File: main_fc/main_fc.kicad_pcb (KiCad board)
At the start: 2 copper layers, 198 parts, among them U1 ADS1158IRTCR, U10 AD8495, U11 AD8495, U12 AD8495, U13 AD8495, U14 AD8495, U15 AD8495, U2 AD8495, U3 OP777ARZ, U4 STM32H730ZBTx, U6 LAN8742A, U7 FT232RL, U8 ADS1158IRTCR, U9 AD8495

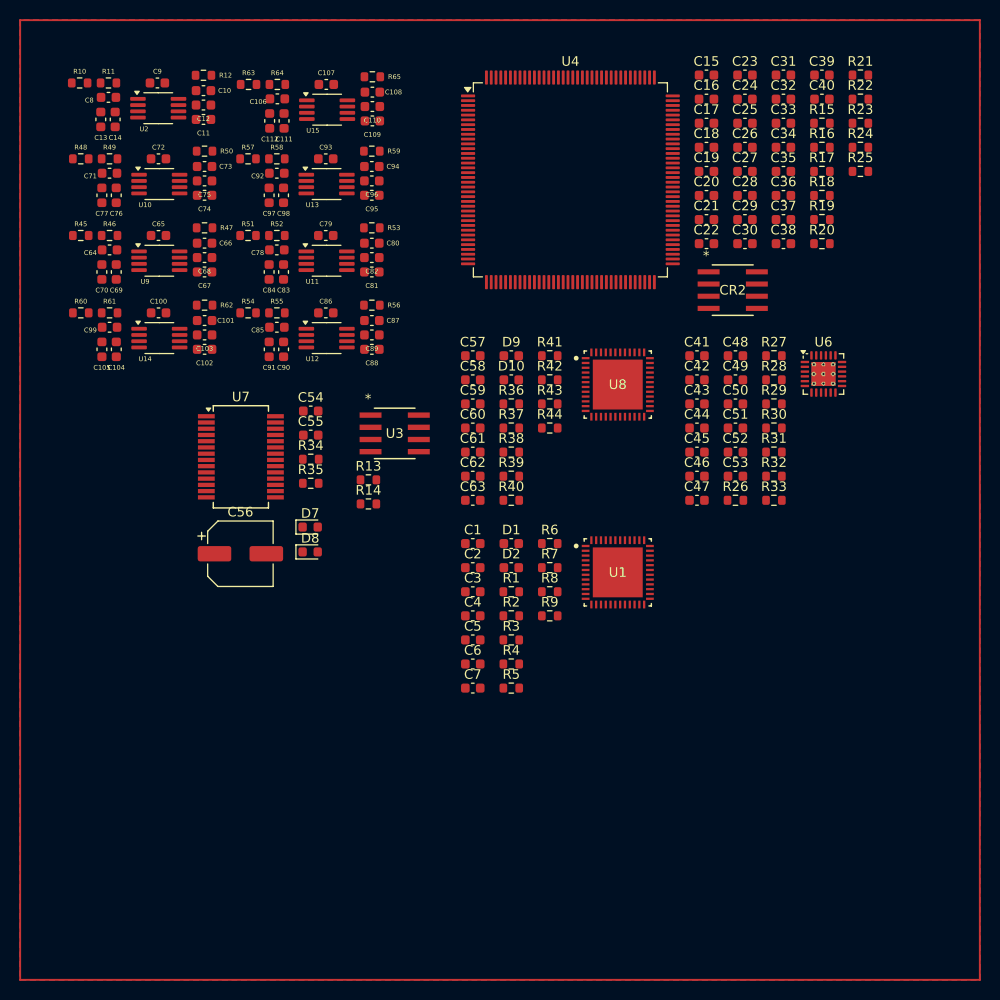
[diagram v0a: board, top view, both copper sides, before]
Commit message: added new stm symbol/footprint
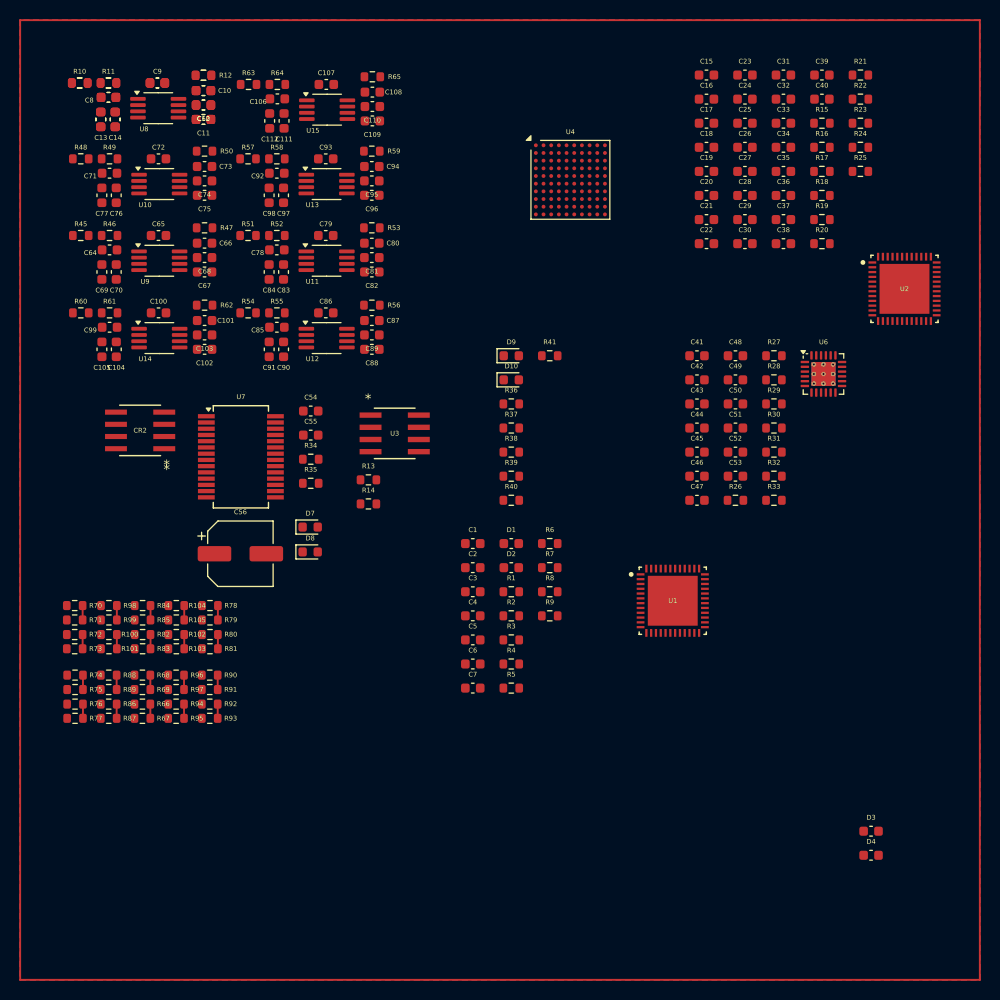
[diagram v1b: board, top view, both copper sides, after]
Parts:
- added D3: LED, Capacitor_SMD:C_0603_1608Metric, F.Cu at (121.7, 113.3)
- added D4: LED, Capacitor_SMD:C_0603_1608Metric, F.Cu at (121.7, 115.8)
- added R100: 2k, Resistor_SMD:R_0603_1608Metric, F.Cu at (42.2, 92.8)
- added R101: 1k, Resistor_SMD:R_0603_1608Metric, F.Cu at (42.2, 94.2)
- added R102: 2k, Resistor_SMD:R_0603_1608Metric, F.Cu at (49.3, 92.8)
- added R103: 1k, Resistor_SMD:R_0603_1608Metric, F.Cu at (49.3, 94.2)
- added R104: 2k, Resistor_SMD:R_0603_1608Metric, F.Cu at (49.3, 89.8)
- added R105: 1k, Resistor_SMD:R_0603_1608Metric, F.Cu at (49.3, 91.2)
- added R66: 2k, Resistor_SMD:R_0603_1608Metric, F.Cu at (45.7, 100.0)
- added R67: 1k, Resistor_SMD:R_0603_1608Metric, F.Cu at (45.7, 101.5)
- added R68: 2k, Resistor_SMD:R_0603_1608Metric, F.Cu at (45.7, 97.0)
- added R69: 1k, Resistor_SMD:R_0603_1608Metric, F.Cu at (45.7, 98.5)
- added R70: 2k, Resistor_SMD:R_0603_1608Metric, F.Cu at (38.7, 89.8)
- added R71: 1k, Resistor_SMD:R_0603_1608Metric, F.Cu at (38.7, 91.2)
- added R72: 2k, Resistor_SMD:R_0603_1608Metric, F.Cu at (38.7, 92.8)
- added R73: 1k, Resistor_SMD:R_0603_1608Metric, F.Cu at (38.7, 94.2)
- added R74: 2k, Resistor_SMD:R_0603_1608Metric, F.Cu at (38.7, 97.0)
- added R75: 1k, Resistor_SMD:R_0603_1608Metric, F.Cu at (38.7, 98.5)
- added R76: 2k, Resistor_SMD:R_0603_1608Metric, F.Cu at (38.7, 100.0)
- added R77: 1k, Resistor_SMD:R_0603_1608Metric, F.Cu at (38.7, 101.5)
- added R78: 2k, Resistor_SMD:R_0603_1608Metric, F.Cu at (52.8, 89.8)
- added R79: 1k, Resistor_SMD:R_0603_1608Metric, F.Cu at (52.8, 91.2)
- added R80: 2k, Resistor_SMD:R_0603_1608Metric, F.Cu at (52.8, 92.8)
- added R81: 1k, Resistor_SMD:R_0603_1608Metric, F.Cu at (52.8, 94.2)
- added R82: 2k, Resistor_SMD:R_0603_1608Metric, F.Cu at (45.8, 92.8)
- added R83: 1k, Resistor_SMD:R_0603_1608Metric, F.Cu at (45.8, 94.2)
- added R84: 2k, Resistor_SMD:R_0603_1608Metric, F.Cu at (45.8, 89.8)
- added R85: 1k, Resistor_SMD:R_0603_1608Metric, F.Cu at (45.8, 91.2)
- added R86: 2k, Resistor_SMD:R_0603_1608Metric, F.Cu at (42.2, 100.0)
- added R87: 1k, Resistor_SMD:R_0603_1608Metric, F.Cu at (42.2, 101.5)
- added R88: 2k, Resistor_SMD:R_0603_1608Metric, F.Cu at (42.2, 97.0)
- added R89: 1k, Resistor_SMD:R_0603_1608Metric, F.Cu at (42.2, 98.5)
- added R90: 2k, Resistor_SMD:R_0603_1608Metric, F.Cu at (52.8, 97.0)
- added R91: 1k, Resistor_SMD:R_0603_1608Metric, F.Cu at (52.8, 98.5)
- added R92: 2k, Resistor_SMD:R_0603_1608Metric, F.Cu at (52.8, 100.0)
- added R93: 1k, Resistor_SMD:R_0603_1608Metric, F.Cu at (52.8, 101.5)
- added R94: 2k, Resistor_SMD:R_0603_1608Metric, F.Cu at (49.2, 100.0)
- added R95: 1k, Resistor_SMD:R_0603_1608Metric, F.Cu at (49.2, 101.5)
- added R96: 2k, Resistor_SMD:R_0603_1608Metric, F.Cu at (49.2, 97.0)
- added R97: 1k, Resistor_SMD:R_0603_1608Metric, F.Cu at (49.2, 98.5)
- added R98: 2k, Resistor_SMD:R_0603_1608Metric, F.Cu at (42.2, 89.8)
- added R99: 1k, Resistor_SMD:R_0603_1608Metric, F.Cu at (42.2, 91.2)
- C10, C9: value 1nF -> 10uF
- C11: value 10uF -> 0.1uF
- C12: value 0.1uF -> 22nf
- C13: value 0.1uF -> 4.7pf
- C14: value 10uF -> 4.7pf
- C57: value 0.1uF -> 1nF
- C58, C59: value 10uF -> 1nF
- C60: value 0.1uF -> 10uF
- C61: value 22nf -> 0.1uF
- C62: value 4.7pf -> 0.1uF
- C63: value 4.7pf -> 10uF
- C8: value 1nF -> 0.1uF
- D10: value LED -> RX_LED; footprint Capacitor_SMD:C_0603_1608Metric -> LED_SMD:LED_0603_1608Metric
- D7: value TX_LED -> LED
- D8: value RX_LED -> LED
- D9: value LED -> TX_LED; footprint Capacitor_SMD:C_0603_1608Metric -> LED_SMD:LED_0603_1608Metric
- R10: value 1M -> 100
- R11: value 10k -> 100
- R13, R14: value 1k -> 10k
- R15: value 200k -> 10k
- R16, R18: value 22 -> 10k
- R17: value 47k -> 10k
- R19: value 47k -> 1k
- R20: value 22 -> 1k
- R21: value 47k -> 200k
- R24: value 47k -> 22
- R26: value 10k -> 22
- R27: value 270 -> 47k
- R28: value 270 -> 22
- R29: value 12.1k -> 47k
- R30, R31: value 49.9 -> 47k
- R32: value 49.9 -> 10k
- R33: value 49.9 -> 270
- R34: value 150 -> 270
- R35: value 150 -> 12.1k
- R36, R37: value 100 -> 49.9
- R38, R39: value 10k -> 49.9
- R40, R41: value 10k -> 150
- R42: value 10k -> 1M
- U2: value AD8495 -> ADS1158IRTCR; footprint Package_SO:MSOP-8_3x3mm_P0.65mm -> avi_footprint:RTC0048A-IPC_C
- U4: value STM32H730ZBTx -> STM32H730VBHx; footprint Package_QFP:LQFP-144_20x20mm_P0.5mm -> Package_BGA:TFBGA-100_8x8mm_Layout10x10_P0.8mm
- U8: value ADS1158IRTCR -> AD8495; footprint avi_footprint:RTC0048A-IPC_C -> Package_SO:MSOP-8_3x3mm_P0.65mm
- moved U2 80.0 mm to (125.1, 56.7)
- moved CR2 63.5 mm to (45.5, 71.5), turned to 180 degrees
- moved R42 57.9 mm to (39.2, 35.3)
- moved R43 56.9 mm to (42.2, 35.3)
- moved U8 55.9 mm to (47.4, 37.9)
- moved C63 55.5 mm to (41.4, 39.1), turned to -90 degrees
- moved C62 52.6 mm to (42.9, 39.1), turned to 90 degrees
- moved R44 51.5 mm to (52.1, 34.5), turned to 180 degrees
- moved C57 46.5 mm to (42.2, 36.8), turned to 180 degrees
- moved C58 45.1 mm to (47.3, 35.3), turned to 180 degrees
- moved C61 44.6 mm to (52.1, 39.1), turned to 180 degrees
- moved C60 43.8 mm to (52.1, 37.6), turned to 180 degrees
- moved C59 43.0 mm to (52.1, 36.1), turned to 180 degrees
- moved U1 6.45 mm to (101.0, 89.2)
- moved C69 1.50 mm to (41.5, 55.0), turned to -90 degrees
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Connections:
- C10 pad 1: GND -> +5V
- C10 pad 2: Net-(U2-+IN) -> GND
- C11 pad 1: GND -> +5V
- C11 pad 2: +5V -> GND
- C12 pad 2: +5V -> Net-(U2-PLLCAP)
- C13 pad 2: GND -> Net-(U2-XTAL1)
- C14 pad 2: GND -> Net-(U2-XTAL2)
- C15 pad 2: Net-(U4-PH0) -> Net-(C15-Pad2)
- C16 pad 2: Net-(U4-PH1) -> Net-(C16-Pad2)
- C18 pad 1: Net-(C18-Pad1) -> unconnected-(C18-Pad1)
- C19 pad 1: Net-(C19-Pad1) -> unconnected-(C19-Pad1)
- C20 pad 1: Net-(U4-PC14) -> Net-(C20-Pad1)
- C21 pad 1: Net-(U4-PC15) -> Net-(C21-Pad1)
- C57 pad 1: +5V -> Net-(U8--IN)
- C58 pad 1: +5V -> Net-(U8-+IN)
- C58 pad 2: GND -> Net-(U8--IN)
- C59 pad 1: +5V -> GND
- C59 pad 2: GND -> Net-(U8-+IN)
- C60 pad 1: +5V -> GND
- C60 pad 2: GND -> +5V
- C61 pad 2: Net-(U8-PLLCAP) -> +5V
- C62 pad 2: Net-(U8-XTAL1) -> GND
- C63 pad 2: Net-(U8-XTAL2) -> GND
- C8 pad 1: Net-(U2--IN) -> +5V
- C9 pad 1: Net-(U2-+IN) -> +5V
- C9 pad 2: Net-(U2--IN) -> GND
- D10 pad 1: GND -> Net-(D10-K)
- D9 pad 1: GND -> Net-(D9-K)
- R10 pad 1: GND -> +5V
- R10 pad 2: /TC0/TC_INPUT- -> Net-(D3-A)
- R11 pad 1: /TC0/TC_INPUT- -> Net-(U2-GPIO0)
- R11 pad 2: Net-(U2--IN) -> Net-(D4-A)
- R12 pad 1: /TC0/TC_INPUT+ -> GND
- R12 pad 2: Net-(U2-+IN) -> Net-(U2-GPIO1)
- R13 pad 1: +5V -> GND
- R13 pad 2: Net-(U3-IN+) -> Net-(U2-GPIO2)
- R14 pad 1: Net-(U3-IN+) -> GND
- R14 pad 2: GND -> Net-(U2-GPIO3)
- R15 pad 1: Net-(U4-PH0) -> GND
- R15 pad 2: Net-(U4-PH1) -> Net-(U2-GPIO4)
- R16 pad 1: SDMMC1_D3 -> GND
- R16 pad 2: Net-(J5-CD/DAT3) -> Net-(U2-GPIO5)
- R17 pad 1: SDMMC1_D3 -> GND
- R17 pad 2: +3V3 -> Net-(U2-GPIO6)
- R18 pad 1: SDMMC1_D2 -> GND
- R18 pad 2: Net-(J5-DAT2) -> Net-(U2-GPIO7)
- R19 pad 1: SDMMC1_D2 -> +5V
- R19 pad 2: +3V3 -> Net-(U3-IN+)
- R20 pad 1: SDMMC1_D1 -> Net-(U3-IN+)
- R20 pad 2: Net-(J5-DAT1) -> GND
- R21 pad 1: SDMMC1_D1 -> Net-(C15-Pad2)
- R21 pad 2: +3V3 -> Net-(C16-Pad2)
- R22 pad 1: SDMMC1_D0 -> SDMMC1_D3
- R23 pad 1: SDMMC1_D0 -> SDMMC1_D3
- R24 pad 1: CARD_DETECT -> SDMMC1_D2
- R24 pad 2: +3V3 -> Net-(J2-DAT2)
- R25 pad 1: WRITE_PROTECT -> SDMMC1_D2
- R26 pad 1: Net-(D3-A) -> SDMMC1_D1
- R26 pad 2: GND -> Net-(J2-DAT1)
- R27 pad 1: Net-(D3-K) -> SDMMC1_D1
- R27 pad 2: GND -> +3V3
- R28 pad 1: Net-(D4-K) -> SDMMC1_D0
- R28 pad 2: GND -> Net-(J2-DAT0)
- R29 pad 1: Net-(U6-RBIAS) -> SDMMC1_D0
- R29 pad 2: GND -> +3V3
- R30 pad 1: +3V3 -> CARD_DETECT
- R30 pad 2: /PHY/ETH_TXD_P -> +3V3
- R31 pad 1: +3V3 -> WRITE_PROTECT
- R31 pad 2: /PHY/ETH_TXD_N -> +3V3
- R32 pad 1: +3V3 -> Net-(D5-A)
- R32 pad 2: /PHY/ETH_RXD_P -> GND
- R33 pad 1: +3V3 -> Net-(D5-K)
- R33 pad 2: /PHY/ETH_RXD_N -> GND
- R34 pad 1: Net-(D7-A) -> Net-(D6-K)
- R35 pad 1: Net-(D8-A) -> Net-(U6-RBIAS)
- R36 pad 1: +5V -> +3V3
- R36 pad 2: Net-(D9-A) -> /PHY/ETH_TXD_P
- R37 pad 1: Net-(U8-GPIO0) -> +3V3
- R37 pad 2: Net-(D10-A) -> /PHY/ETH_TXD_N
- R38 pad 1: GND -> +3V3
- R38 pad 2: Net-(U8-GPIO1) -> /PHY/ETH_RXD_P
- R39 pad 1: GND -> +3V3
- R39 pad 2: Net-(U8-GPIO2) -> /PHY/ETH_RXD_N
- R40 pad 1: GND -> Net-(D9-A)
- R40 pad 2: Net-(U8-GPIO3) -> GND
- R41 pad 1: GND -> Net-(D10-A)
- R41 pad 2: Net-(U8-GPIO4) -> GND
- R42 pad 2: Net-(U8-GPIO5) -> /TC0/TC_INPUT-
- R43 pad 1: GND -> /TC0/TC_INPUT-
- R43 pad 2: Net-(U8-GPIO6) -> Net-(U8--IN)
- R44 pad 1: GND -> /TC0/TC_INPUT+
- R44 pad 2: Net-(U8-GPIO7) -> Net-(U8-+IN)
- U2 pad 1: Net-(U2--IN) -> /ADC1/AIN3
- U2 pad 2: /BUF_2V5 -> /ADC1/AIN2
- U2 pad 3: GND -> /ADC1/AIN1
- U2 pad 4: unconnected-(U2-NC-Pad4) -> /ADC1/AIN0
- U2 pad 5: /TC0/TC_OUT -> GND
- U2 pad 6: /TC0/TC_OUT -> +5V
- U2 pad 7: +5V -> Net-(U2-PLLCAP)
- U2 pad 8: Net-(U2-+IN) -> Net-(U2-XTAL1)
- U6 pad 2: Net-(D3-A) -> Net-(D5-A)
- U7 pad 22: Net-(D8-K) -> Net-(D10-K)
- U7 pad 23: Net-(D7-K) -> Net-(D9-K)
- U8 pad 1: /ADC1/AIN3 -> Net-(U8--IN)
- U8 pad 2: /ADC1/AIN2 -> /BUF_2V5
- U8 pad 3: /ADC1/AIN1 -> GND
- U8 pad 4: /ADC1/AIN0 -> unconnected-(U8-NC-Pad4)
- U8 pad 5: GND -> /TC0/TC_OUT
- U8 pad 6: +5V -> /TC0/TC_OUT
- U8 pad 7: Net-(U8-PLLCAP) -> +5V
- U8 pad 8: Net-(U8-XTAL1) -> Net-(U8-+IN)
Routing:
- net /PT_Divider9/OUTPUT-: track 0.00 -> 1.50 mm
- net /PT_Divider8/OUTPUT+: track 0.00 -> 1.50 mm
- net /PT_Divider7/OUTPUT-: track 0.00 -> 1.50 mm
- net /PT_Divider6/OUTPUT+: track 0.00 -> 1.50 mm
- net /PT_Divider5/OUTPUT-: track 0.00 -> 1.50 mm
- net /PT_Divider4/OUTPUT-: track 0.00 -> 1.50 mm
- net /PT_Divider3/OUTPUT+: track 0.00 -> 1.50 mm
- net /PT_Divider2/OUTPUT+: track 0.00 -> 1.50 mm
- net /PT_Divider1/OUTPUT+: track 0.00 -> 1.50 mm
- net /PT_Divider0/OUTPUT-: track 0.00 -> 1.50 mm
- net /PT_Divider9/OUTPUT+: track 0.00 -> 1.48 mm
- net /PT_Divider8/OUTPUT-: track 0.00 -> 1.48 mm
- net /PT_Divider7/OUTPUT+: track 0.00 -> 1.48 mm
- net /PT_Divider6/OUTPUT-: track 0.00 -> 1.48 mm
- net /PT_Divider5/OUTPUT+: track 0.00 -> 1.48 mm
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
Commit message: updated board dimensions
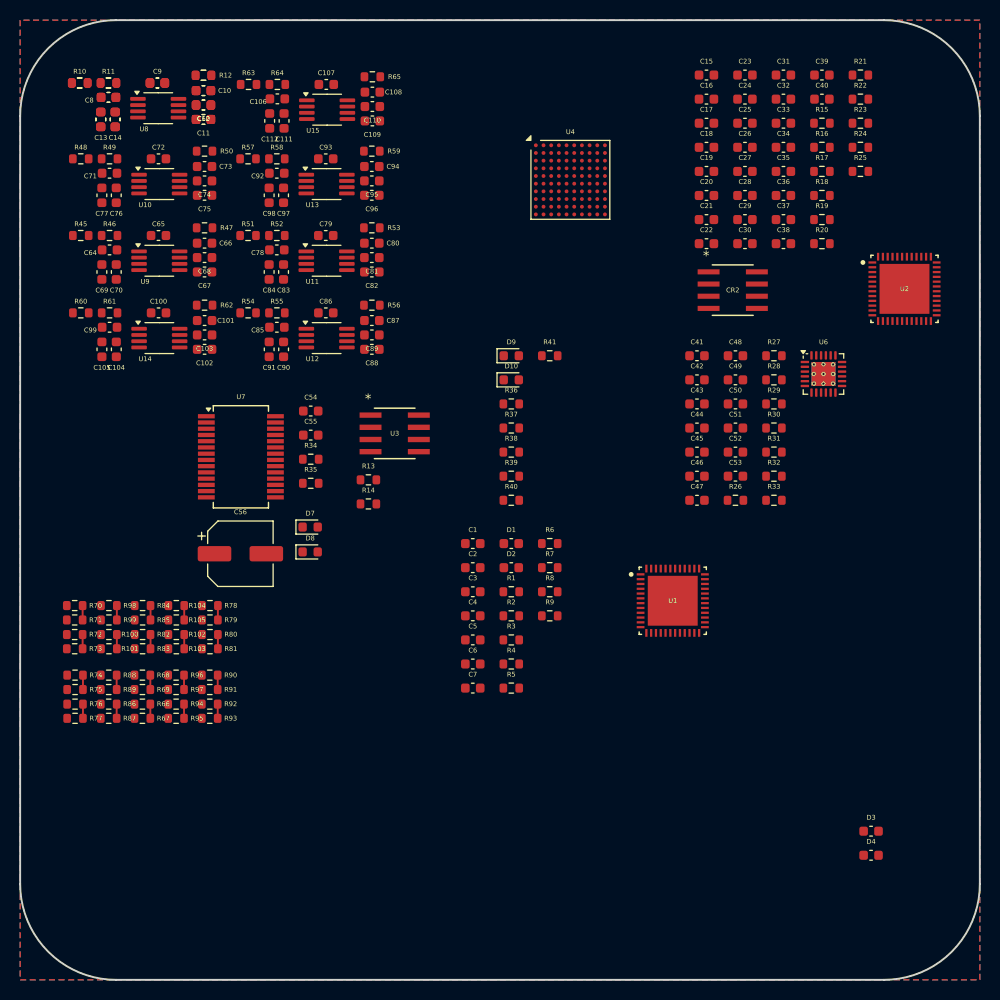
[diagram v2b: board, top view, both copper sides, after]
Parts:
- moved CR2 63.5 mm to (107.3, 56.9), turned to 0 degrees
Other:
- board outline added: 100 x 100 mm

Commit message: Added footprints for stm sheet to lib folder
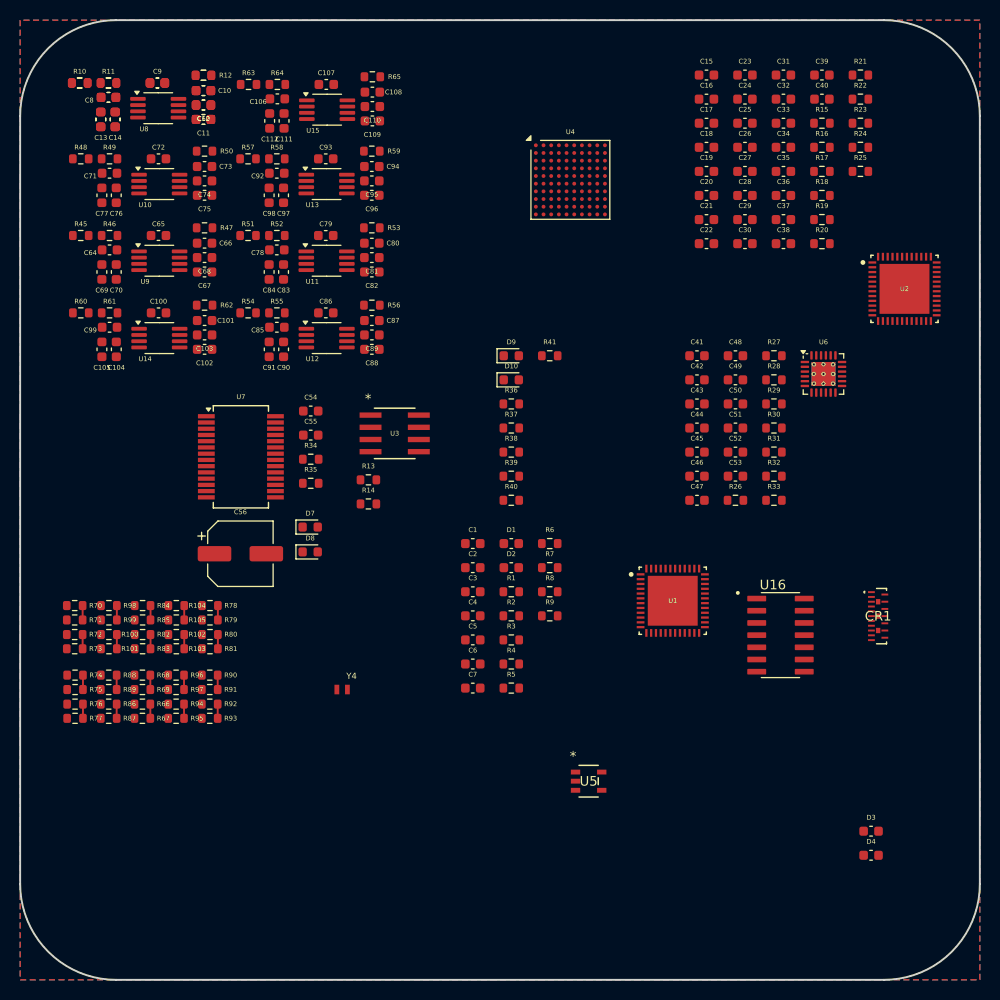
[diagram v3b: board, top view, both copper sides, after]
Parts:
- removed CR2: ST485BDR, avi_footprint:SO-8_STM-M
- added CR1: ESD7008MUTAG, ESD7008MUTAG:UDFN18_517BV_ONS, F.Cu at (122.4, 90.8)
- added U16: MAX13448EESD_, MAX13448EESD_:SOIC127P600X175-14N, F.Cu at (112.2, 92.8)
- added U5: REF4132B25DBVR, REF4132B25DBVR:SOT-23-5_DBV_TEX, F.Cu at (92.2, 108.0)
- added Y4: ABS05-32.768KHZ-T, ABS05-32.768KHZ-T:XTAL_ABS05-32.768KHZ-T, F.Cu at (66.5, 98.5)
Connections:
- C23 pad 1: /STM/MCU_VDDA -> +3V3
- C25 pad 1: /STM/MCU_VDDA -> +3V3
- U4 pad B2: unconnected-(U4-VBAT-PadB2) -> +3V3
- U4 pad C2: Net-(U4-VSS-PadC2) -> GND
- U4 pad D2: unconnected-(U4-VDD-PadD2) -> +3V3
- U4 pad E4: Net-(U4-VSS-PadC2) -> GND
- U4 pad E5: Net-(U4-VSS-PadC2) -> GND
- U4 pad E6: Net-(U4-VSS-PadC2) -> GND
- U4 pad F4: unconnected-(U4-VDD-PadF4) -> +3V3
- U4 pad F5: unconnected-(U4-VDD-PadF5) -> +3V3
- U4 pad F6: unconnected-(U4-VDD33USB-PadF6) -> +3V3
- U4 pad G1: unconnected-(U4-VSSA-PadG1) -> GND
- U4 pad H1: unconnected-(U4-VDDA-PadH1) -> +3V3
- U4 pad J1: Net-(U4-VSS-PadC2) -> GND
- U4 pad K1: unconnected-(U4-VDD-PadK1) -> +3V3
